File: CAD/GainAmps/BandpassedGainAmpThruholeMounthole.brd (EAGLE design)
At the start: 7.4 x 16.1 mm, 9 parts, among them U1 OPA202IDGKR

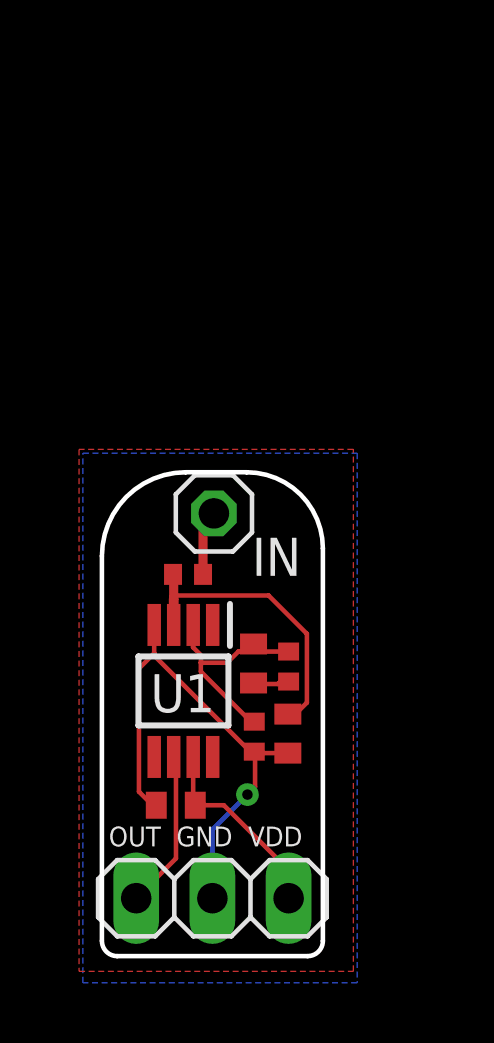
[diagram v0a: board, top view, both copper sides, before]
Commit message: moved, added production files for gain amps
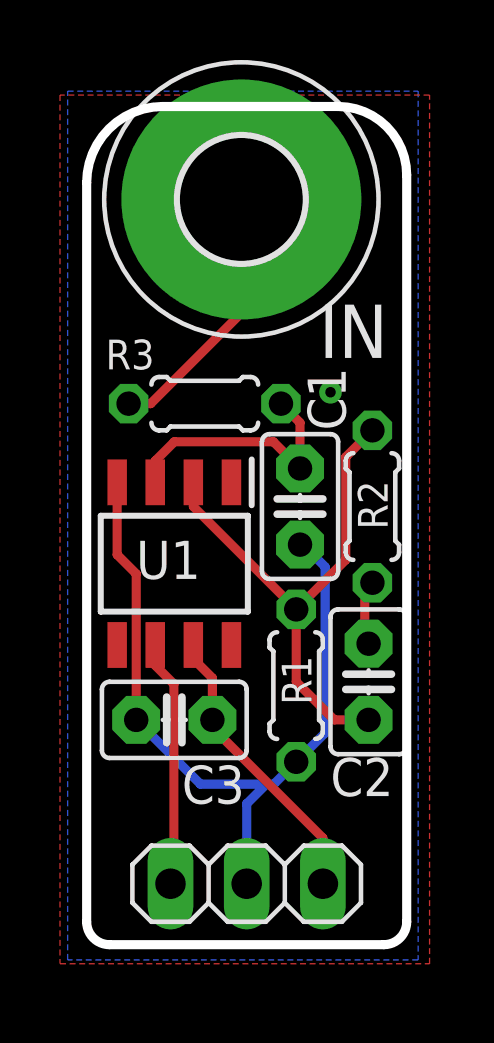
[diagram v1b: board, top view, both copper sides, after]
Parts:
- removed IN: (no value), pinhead:1X01
- added H1: MOUNT-PAD-ROUND4.1, holes:4,1-PAD
- C1, C2, C3: device rcl:C0402 -> capacitor-wima:C2.5-2
- R1, R2, R3: device rcl:R0402 -> rcl:0204/5
- U1: value OPA202IDGKR -> OPA202IDR; device OPA202IDGKR:SOP65P490X110-8N -> OPA202IDR:SOIC127P600X175-8N
- moved C1 7.58 mm to (8.13, 16.6)
- moved R2 6.02 mm to (10.5, 16.6)
- moved R3 5.72 mm to (4.95, 20.1), turned to 0 degrees
- moved U1 4.25 mm to (3.94, 14.7)
- moved C2 3.88 mm to (10.4, 10.8), turned to 90 degrees
- moved C3 2.85 mm to (3.94, 9.53), turned to 180 degrees
- moved R1 2.20 mm to (8.00, 10.7)
- moved JP1 1.24 mm to (6.35, 4.06)
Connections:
- net GND: now also C3.2; no longer C3.1
- net IN: now also H1.B4,1; no longer IN.1
- net VDD: now also C3.1; no longer C3.2
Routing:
- net -IN: track 8.01 -> 18.0 mm
- net GND: track 18.0 -> 26.3 mm
- net IN: track 2.18 -> 8.80 mm
- net VDD: track 6.58 -> 9.75 mm
- net +IN: track 11.7 -> 8.60 mm
- net OUT: track 5.29 -> 8.29 mm
- net N$3: track 1.47 -> 2.19 mm
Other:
- board size 7.4 x 16.1 mm -> 10.7 x 27.9 mm
- board text added: "VDD GND OUT"
- board text removed: "OUT GND VDD"

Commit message: fixed edge plating
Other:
- board size 10.7 x 27.9 mm -> 10.7 x 26.9 mm
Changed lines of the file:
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@@
 <board>
 <plain>
-<wire x1="10.922" y1="2.032" x2="1.778" y2="2.032" width="0.3048" layer="20"/>
-<wire x1="1.778" y1="2.032" x2="1.016" y2="2.794" width="0.3048" layer="20" curve="-90"/>
-<wire x1="1.016" y1="2.794" x2="1.016" y2="27.432" width="0.3048" layer="20"/>
+<wire x1="10.922" y1="3.048" x2="1.778" y2="3.048" width="0.3048" layer="20"/>
+<wire x1="1.778" y1="3.048" x2="1.016" y2="3.81" width="0.3048" layer="20" curve="-90"/>
+<wire x1="1.016" y1="3.81" x2="1.016" y2="27.432" width="0.3048" layer="20"/>
 <wire x1="1.016" y1="27.432" x2="3.556" y2="29.972" width="0.3048" layer="20" curve="-90"/>
 <wire x1="3.556" y1="29.972" x2="9.398" y2="29.972" width="0.3048" layer="20"/>
 <wire x1="9.398" y1="29.972" x2="11.684" y2="27.686" width="0.3048" layer="20" curve="-90"/>
-<wire x1="11.684" y1="27.686" x2="11.684" y2="2.794" width="0.3048" layer="20"/>
-<wire x1="11.684" y1="2.794" x2="10.922" y2="2.032" width="0.3048" layer="20" curve="-90"/>
+<wire x1="11.684" y1="27.686" x2="11.684" y2="3.81" width="0.3048" layer="20"/>
+<wire x1="11.684" y1="3.81" x2="10.922" y2="3.048" width="0.3048" layer="20" curve="-90"/>
 <text x="11.303" y="21.59" size="1.778" layer="26" rot="MR0">IN</text>
 <text x="1.397" y="6.858" size="1.016" layer="26" rot="MR180">VDD GND OUT</text>
-<dimension x1="1.778" y1="2.032" x2="3.556" y2="29.972" x3="-1.397" y3="16.002" textsize="1.778" layer="47" dtype="vertical"/>
 <dimension x1="1.016" y1="27.432" x2="11.684" y2="27.686" x3="6.35" y3="33.147" textsize="1.778" layer="47" dtype="horizontal"/>
 <text x="8.763" y="21.59" size="1.778" layer="25">IN</text>
+<dimension x1="3.556" y1="29.972" x2="1.778" y2="3.048" x3="-0.762" y3="16.51" textsize="1.778" layer="47" dtype="vertical"/>
 </plain>
 <attributes>
@@
 <wire x1="6.35" y1="6.731" x2="6.35" y2="4.064" width="0.3048" layer="16"/>
 <polygon width="0.3048" layer="1">
-<vertex x="0.127" y="1.397"/>
-<vertex x="12.446" y="1.397"/>
-<vertex x="12.446" y="30.353"/>
-<vertex x="0.127" y="30.353"/>
+<vertex x="0.127" y="2.413"/>
+<vertex x="12.446" y="2.413"/>
+<vertex x="12.446" y="31.369"/>
+<vertex x="0.127" y="31.369"/>
 </polygon>
 <polygon width="0.3048" layer="16">
-<vertex x="0.381" y="1.524"/>
-<vertex x="0.381" y="30.48"/>
-<vertex x="12.065" y="30.48"/>
-<vertex x="12.065" y="1.524"/>
+<vertex x="0.381" y="2.54"/>
+<vertex x="0.381" y="31.496"/>
+<vertex x="12.065" y="31.496"/>
+<vertex x="12.065" y="2.54"/>
 </polygon>
 <via x="9.144" y="20.447" extent="1-16" drill="0.35"/>

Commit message: fixes
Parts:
- removed R3: 1K, rcl:0204/5
- added REF: (no value), pinhead:1X01
- moved R1 6.99 mm to (7.75, 17.7), turned to 270 degrees
- moved R2 6.25 mm to (7.75, 11.0)
- moved C1 2.10 mm to (10.0, 17.5), turned to 270 degrees
- moved C2 0.74 mm to (10.0, 11.4), turned to 270 degrees
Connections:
- removed net -IN: C2.1, R1.2, R2.1, U1.2
- removed net N$3: C2.2, R2.2
- new net +REF: REF.1, U1.2
- new net R1C1: C1.1, R1.2
- net +IN: now also C2.1, R2.1; no longer R3.2
- net GND: now also JP1.3; no longer C1.1, JP1.2, R1.1
- net IN: now also R1.1; no longer R3.1
- net OUT: now also C2.2, JP1.1, R2.2; no longer JP1.3
- net VDD: now also JP1.2; no longer JP1.1
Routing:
- net -IN: track 18.0 -> 0.00 mm
- net GND: track 26.3 -> 14.1 mm
- net OUT: track 8.29 -> 17.2 mm
- net R1C1: track 0.00 -> 4.63 mm
- net +IN: track 8.60 -> 12.8 mm
- net +REF: track 0.00 -> 3.74 mm
- net N$3: track 2.19 -> 0.00 mm
- net IN: track 8.80 -> 7.33 mm
- net VDD: track 9.75 -> 9.16 mm
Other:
- board text added: "GND VDD OUT"
- board text removed: "VDD GND OUT"
